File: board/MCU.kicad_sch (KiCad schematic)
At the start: 28 parts, among them SW1 SW_Push, SW2 SW_Push, U1 STSPIN32G4TR

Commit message: Tentatively finished rev1.
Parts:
- C18, C23: footprint Capacitor_SMD:C_0402_1005Metric_Pad0.74x0.62mm_HandSolder -> Capacitor_SMD:C_0603_1608Metric_Pad1.08x0.95mm_HandSolder
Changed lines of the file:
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@@
 	(wire
 		(pts
-			(xy 96.52 119.38) (xy 99.06 119.38)
+			(xy 77.47 119.38) (xy 99.06 119.38)
 		)
 		(stroke
@@
 	(wire
 		(pts
-			(xy 96.52 116.84) (xy 99.06 116.84)
+			(xy 77.47 116.84) (xy 99.06 116.84)
 		)
 		(stroke
@@
 			(width 0)
 			(type default)
+		)
+	)
+	(label "CANX+"
+		(at 78.74 119.38 0)
+		(effects
+			(font
+				(size 1.27 1.27)
+			)
+			(justify left bottom)
+		)
+	)
+	(label "CANX-"
+		(at 78.74 116.84 0)
+		(effects
+			(font
+				(size 1.27 1.27)
+			)
+			(justify left bottom)
 		)
 	)
@@
 	(hierarchical_label "CAN_RX"
 		(shape input)
-		(at 96.52 116.84 180)
+		(at 77.47 116.84 180)
 		(effects
 			(font
@@
 	(hierarchical_label "CAN_TX"
 		(shape output)
-		(at 96.52 119.38 180)
+		(at 77.47 119.38 180)
 		(effects
 			(font
@@
 			)
 		)
-		(property "Footprint" "Capacitor_SMD:C_0402_1005Metric_Pad0.74x0.62mm_HandSolder"
+		(property "Footprint" "Capacitor_SMD:C_0603_1608Metric_Pad1.08x0.95mm_HandSolder"
 			(at 201.93 93.0148 0)
 			(effects
@@
 			)
 		)
-		(property "Footprint" "Capacitor_SMD:C_0402_1005Metric_Pad0.74x0.62mm_HandSolder"
+		(property "Footprint" "Capacitor_SMD:C_0603_1608Metric_Pad1.08x0.95mm_HandSolder"
 			(at 201.93 75.2348 0)
 			(effects

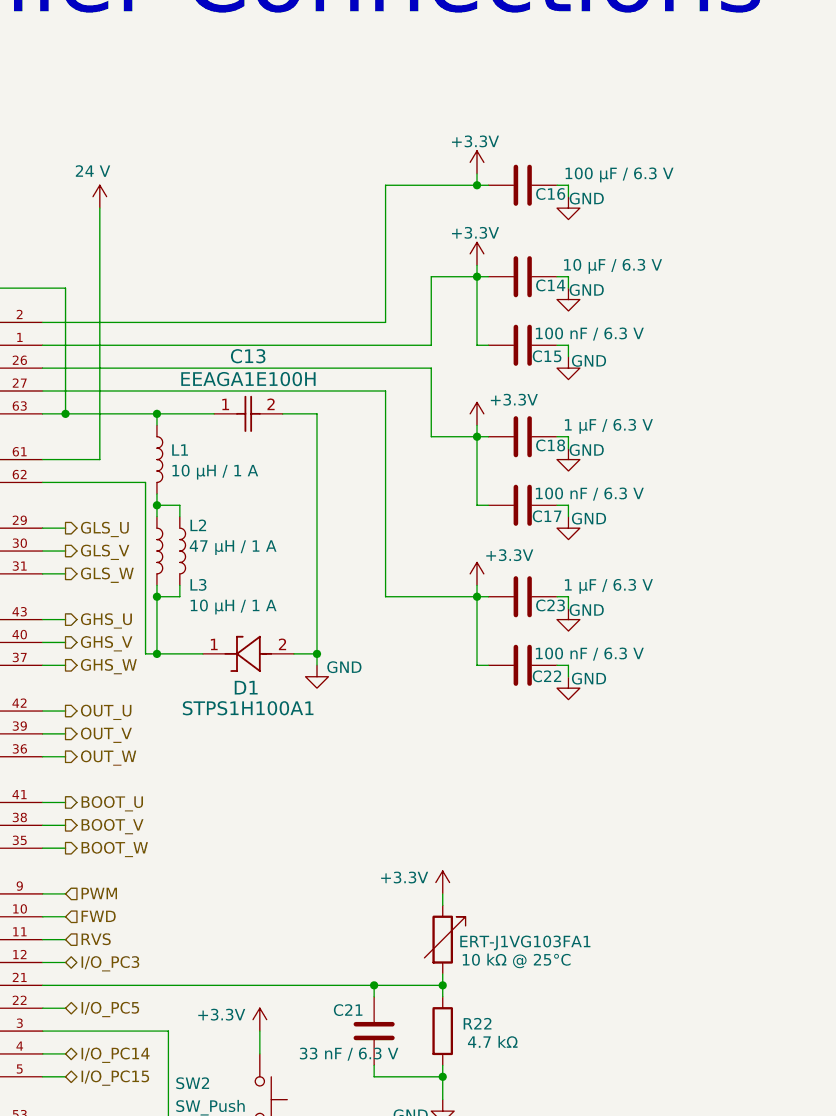
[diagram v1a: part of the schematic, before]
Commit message: Fixed many issues found in Rev1 review prior to order
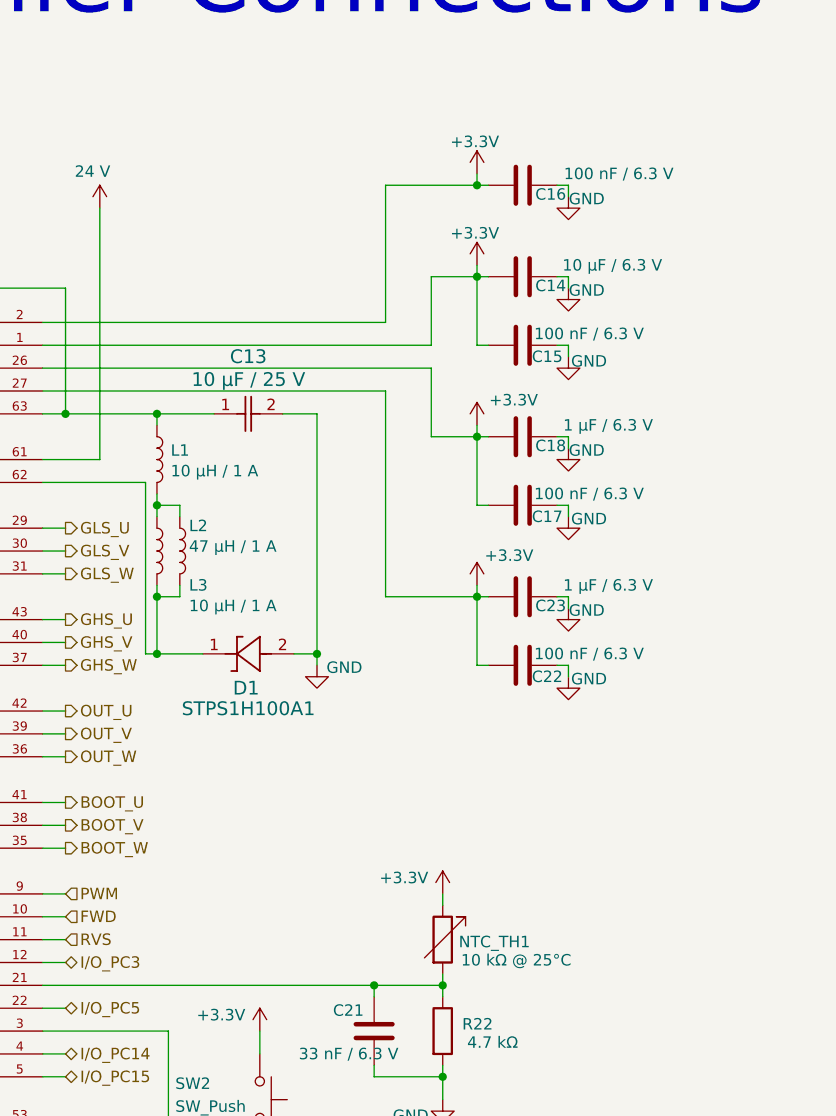
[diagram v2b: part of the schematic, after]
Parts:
- C13: value EEAGA1E100H -> 10 µF / 25 V
- C16: value 100 μF / 6.3 V -> 100 nF / 6.3 V; footprint Capacitor_SMD:C_1206_3216Metric_Pad1.33x1.80mm_HandSolder -> Capacitor_SMD:C_0603_1608Metric_Pad1.08x0.95mm_HandSolder
- renumbered ERT-J1VG103FA1 to NTC_TH1
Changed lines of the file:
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@@
 			)
 		)
-		(property "Value" "100 μF / 6.3 V"
+		(property "Value" "100 nF / 6.3 V"
 			(at 214.884 46.99 90)
 			(effects
@@
 			)
 		)
-		(property "Footprint" "Capacitor_SMD:C_1206_3216Metric_Pad1.33x1.80mm_HandSolder"
+		(property "Footprint" "Capacitor_SMD:C_0603_1608Metric_Pad1.08x0.95mm_HandSolder"
 			(at 201.93 47.2948 0)
 			(effects
@@
 		(on_board yes)
 		(dnp no)
-		(property "Reference" "ERT-J1VG103FA1"
+		(property "Reference" "NTC_TH1"
 			(at 191.008 132.334 0)
 			(effects
@@
 			(project "BrushlessMocoBoard"
 				(path "/1ef8bc88-f0df-4a97-862b-c4b9ec3b4ed0/02edeb2f-867a-4e66-ac0c-df2434256428"
-					(reference "ERT-J1VG103FA1")
+					(reference "NTC_TH1")
 					(unit 1)
 				)
@@
 			)
 		)
-		(property "Value" "EEAGA1E100H"
+		(property "Value" "10 µF / 25 V"
 			(at 167.64 69.85 0)
 			(effects

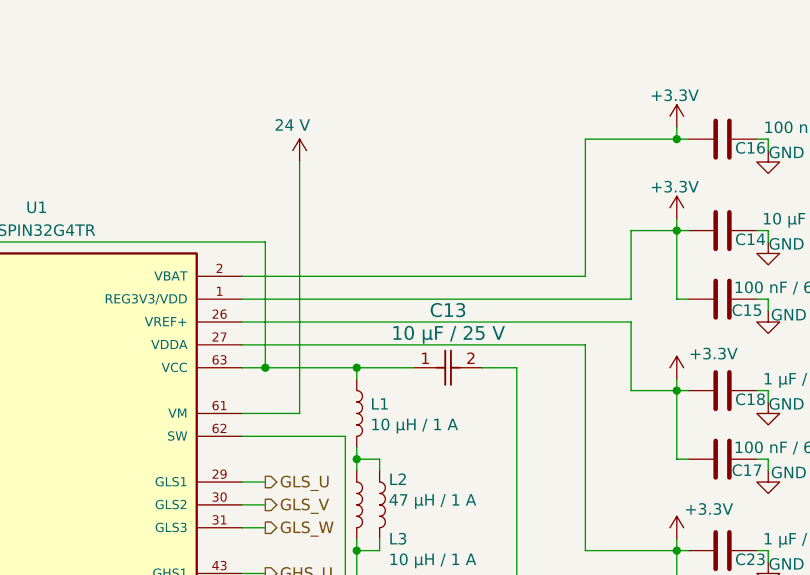
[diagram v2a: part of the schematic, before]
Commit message: Added Cvm to schematic, need to add to layout as well
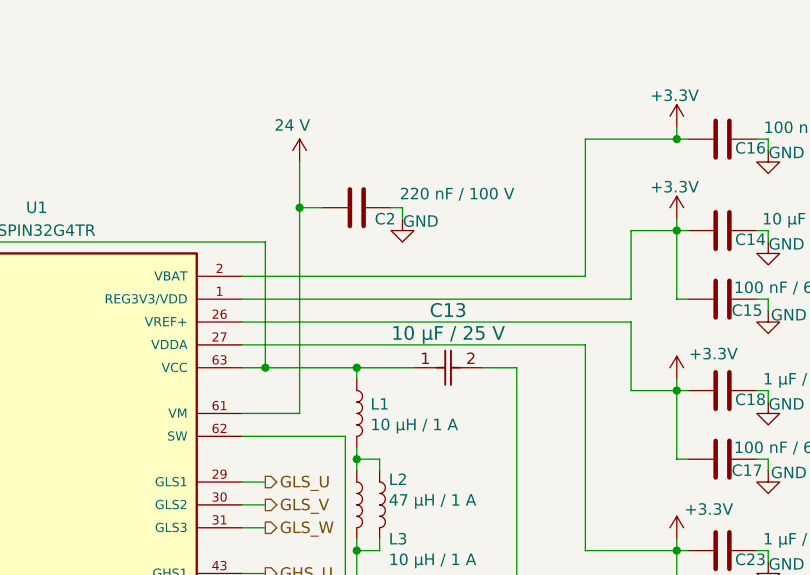
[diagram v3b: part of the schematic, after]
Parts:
- added C2: 220 nF / 100 V, Capacitor_SMD:C_0603_1608Metric_Pad1.08x0.95mm_HandSolder, symbol Device:C
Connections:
- net 24 V: now also C2.1
- net GND: now also C2.2
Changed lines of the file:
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@@
 	)
 	(junction
+		(at 151.13 55.88)
+		(diameter 0)
+		(color 0 0 0 0)
+	)
+	(junction
 		(at 175.26 100.33)
 		(diameter 0)
@@
 	(wire
 		(pts
-			(xy 151.13 50.8) (xy 151.13 78.74)
+			(xy 151.13 50.8) (xy 151.13 55.88)
 		)
 		(stroke
@@
 	(wire
 		(pts
+			(xy 162.56 55.88) (xy 162.56 57.15)
+		)
+		(stroke
+			(width 0)
+			(type default)
+		)
+	)
+	(wire
+		(pts
 			(xy 96.52 152.4) (xy 99.06 152.4)
 		)
@@
 	(wire
 		(pts
+			(xy 153.67 55.88) (xy 151.13 55.88)
+		)
+		(stroke
+			(width 0)
+			(type default)
+		)
+	)
+	(wire
+		(pts
 			(xy 92.71 72.39) (xy 82.55 72.39)
 		)
@@
 	(wire
 		(pts
+			(xy 161.29 55.88) (xy 162.56 55.88)
+		)
+		(stroke
+			(width 0)
+			(type default)
+		)
+	)
+	(wire
+		(pts
 			(xy 203.2 58.42) (xy 201.93 58.42)
 		)
@@
 	(wire
 		(pts
+			(xy 151.13 55.88) (xy 151.13 78.74)
+		)
+		(stroke
+			(width 0)
+			(type default)
+		)
+	)
+	(wire
+		(pts
 			(xy 96.52 104.14) (xy 99.06 104.14)
 		)
@@
 	(symbol
 		(lib_id "Device:C")
+		(at 157.48 55.88 90)
+		(unit 1)
+		(exclude_from_sim no)
+		(in_bom yes)
+		(on_board yes)
+		(dnp no)
+		(property "Reference" "C2"
+			(at 161.798 57.15 90)
+			(effects
+				(font
+					(size 1.27 1.27)
+				)
+				(justify left)
+			)
+		)
+		(property "Value" "220 nF / 100 V"
+			(at 175.006 54.356 90)
+			(effects
+				(font
+					(size 1.27 1.27)
+				)
+				(justify left)
+			)
+		)
+		(property "Footprint" "Capacitor_SMD:C_0603_1608Metric_Pad1.08x0.95mm_HandSolder"
+			(at 161.29 54.9148 0)
+			(effects
+				(font
+					(size 1.27 1.27)
+				)
+				(hide yes)
+			)
+		)
+		(property "Datasheet" "~"
+			(at 157.48 55.88 0)
+			(effects
+				(font
+					(size 1.27 1.27)
+				)
+				(hide yes)
+			)
+		)
+		(property "Description" "Unpolarized capacitor"
+			(at 157.48 55.88 0)
+			(effects
+				(font
+					(size 1.27 1.27)
+				)
+				(hide yes)
+			)
+		)
+		(pin "1"
+		)
+		(pin "2"
+		)
+		(instances
+			(project "BrushlessMocoBoard"
+				(path "/1ef8bc88-f0df-4a97-862b-c4b9ec3b4ed0/02edeb2f-867a-4e66-ac0c-df2434256428"
+					(reference "C2")
+					(unit 1)
+				)
+			)
+		)
+	)
+	(symbol
+		(lib_id "Device:C")
 		(at 198.12 48.26 90)
 		(unit 1)
@@
 					(unit 1)
 				)
+			)
+		)
+	)
+	(symbol
+		(lib_id "power:GND")
+		(at 162.56 57.15 0)
+		(unit 1)
+		(exclude_from_sim no)
+		(in_bom yes)
+		(on_board yes)
+		(dnp no)
+		(property "Reference" "#PWR02"
+			(at 162.56 63.5 0)
+			(effects
+				(font
+					(size 1.27 1.27)
+				)
+				(hide yes)
+			)
+		)
+		(property "Value" "GND"
+			(at 164.592 57.404 0)
+			(effects
+				(font
+					(size 1.27 1.27)
+				)
+			)
+		)
+		(property "Footprint" ""
+			(at 162.56 57.15 0)
+			(effects
+				(font
+					(size 1.27 1.27)
+				)
+				(hide yes)
+			)
+		)
+		(property "Datasheet" ""
+			(at 162.56 57.15 0)
+			(effects
+				(font
+					(size 1.27 1.27)
+				)
+				(hide yes)
+			)
+		)
+		(property "Description" "Power symbol creates a global label with name \"GND\" , ground"
+			(at 162.56 57.15 0)
+			(effects
+				(font
+					(size 1.27 1.27)
+				)
+				(hide yes)
+			)
+		)
+		(pin "1"
+		)
+		(instances
+			(project "BrushlessMocoBoard"
+				(path "/1ef8bc88-f0df-4a97-862b-c4b9ec3b4ed0/02edeb2f-867a-4e66-ac0c-df2434256428"
+					(reference "#PWR02")
+					(unit 1)
+				)

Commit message: Added footprints to board library
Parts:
- STPS1H100A1: footprint BoCoFootprintLibrary:SMA_STM -> BrushlessMocoBoard:SMA_STM
- U1: footprint STSPIN32G4TR:QFN50P900X900X100-65N -> BrushlessMocoBoard:QFN50P900X900X100-65N
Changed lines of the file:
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@@
 			)
 		)
-		(property "Footprint" "BoCoFootprintLibrary:SMA_STM"
+		(property "Footprint" "BrushlessMocoBoard:SMA_STM"
 			(at 172.72 100.33 0)
 			(effects
@@
 			)
 		)
-		(property "Footprint" "STSPIN32G4TR:QFN50P900X900X100-65N"
+		(property "Footprint" "BrushlessMocoBoard:QFN50P900X900X100-65N"
 			(at 121.92 116.84 0)
 			(effects
